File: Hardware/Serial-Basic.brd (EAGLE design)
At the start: 22.9 x 17.3 mm, 24 parts, among them J1 microB, U1 AP2112-3.3V, U2 CH340G, Y2 12MHz

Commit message: Adding buffer to RX line.
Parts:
- added U4: 7408, Serial-Basic:SOT353
- moved JP3 14.9 mm to (3.81, 16.0)
- moved JP4 12.8 mm to (21.5, 1.40)
- moved LOGO3 0.38 mm to (8.89, -0.13)
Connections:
- new net N$5: D2.C, U4.4
- new net SHLD: J1.SHIELD1, J1.SHIELD2, J1.SHIELD3
- net GND: now also U4.3
- net RXI: now also U4.1, U4.2; no longer D2.C
- net VCC: now also U4.5
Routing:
- net VCC: track 49.9 -> 44.2 mm
- net N$5: track 0.00 -> 1.95 mm
- net RXI: track 27.5 -> 29.0 mm
- net TXO: track 24.5 -> 25.1 mm
- net GND: vias 9 -> 11

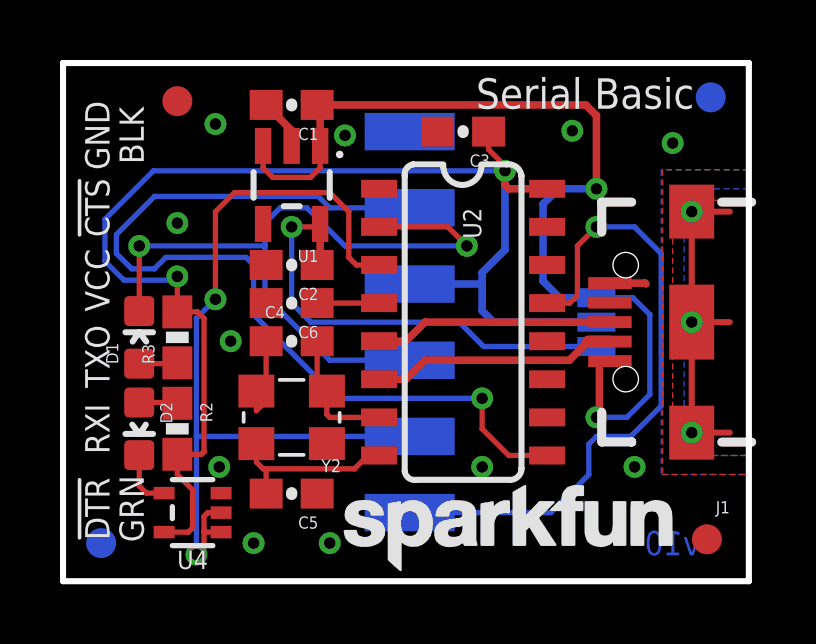
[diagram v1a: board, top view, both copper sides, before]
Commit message: Adding PROD_ID to AND gate
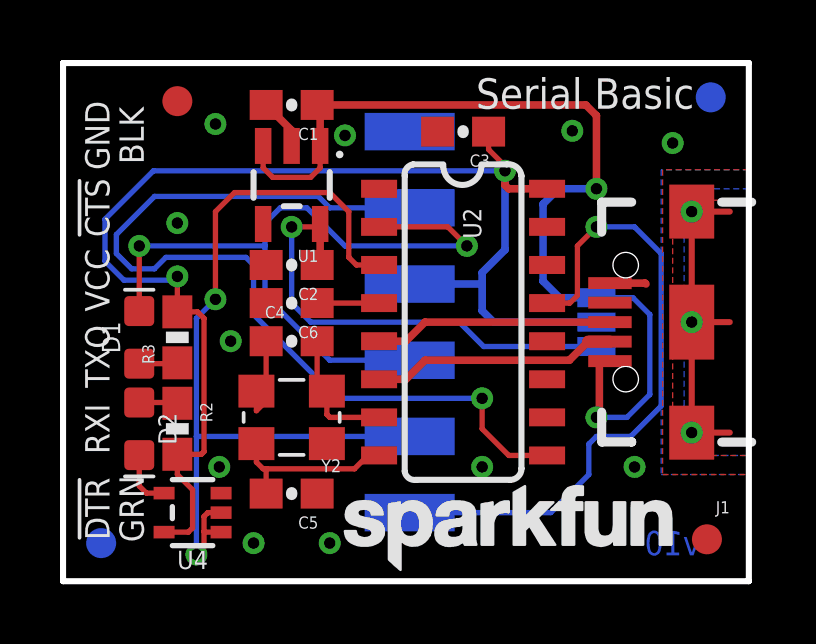
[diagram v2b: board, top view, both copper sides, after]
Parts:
- U4: value 7408 -> 74LVC1G08SE
- turned D1 to 90 degrees
- turned D2 to 270 degrees
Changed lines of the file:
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@@
 <?xml version="1.0" encoding="utf-8"?>
 <!DOCTYPE eagle SYSTEM "eagle.dtd">
-<eagle version="7.6.0">
+<eagle version="7.2.0">
 <drawing>
 <settings>
@@
 <layer number="20" name="Dimension" color="15" fill="1" visible="yes" active="yes"/>
 <layer number="21" name="tPlace" color="16" fill="1" visible="yes" active="yes"/>
-<layer number="22" name="bPlace" color="14" fill="1" visible="no" active="yes"/>
+<layer number="22" name="bPlace" color="14" fill="1" visible="yes" active="yes"/>
 <layer number="23" name="tOrigins" color="15" fill="1" visible="yes" active="yes"/>
-<layer number="24" name="bOrigins" color="15" fill="1" visible="no" active="yes"/>
-<layer number="25" name="tNames" color="7" fill="1" visible="yes" active="yes"/>
+<layer number="24" name="bOrigins" color="15" fill="1" visible="yes" active="yes"/>
+<layer number="25" name="tNames" color="7" fill="1" visible="no" active="yes"/>
 <layer number="26" name="bNames" color="7" fill="1" visible="no" active="yes"/>
 <layer number="27" name="tValues" color="7" fill="1" visible="no" active="yes"/>
@@
 <layer number="43" name="vRestrict" color="2" fill="10" visible="no" active="yes"/>
 <layer number="44" name="Drills" color="7" fill="1" visible="no" active="yes"/>
-<layer number="45" name="Holes" color="7" fill="1" visible="no" active="yes"/>
+<layer number="45" name="Holes" color="7" fill="1" visible="yes" active="yes"/>
 <layer number="46" name="Milling" color="3" fill="1" visible="no" active="yes"/>
 <layer number="47" name="Measures" color="7" fill="1" visible="no" active="yes"/>
@@
 <layer number="49" name="Reference" color="7" fill="1" visible="no" active="yes"/>
 <layer number="50" name="dxf" color="7" fill="1" visible="no" active="yes"/>
-<layer number="51" name="tDocu" color="6" fill="1" visible="no" active="yes"/>
+<layer number="51" name="tDocu" color="6" fill="1" visible="yes" active="yes"/>
 <layer number="52" name="bDocu" color="7" fill="1" visible="no" active="yes"/>
 <layer number="53" name="tGND_GNDA" color="7" fill="9" visible="no" active="no"/>
@@
 <element name="LOGO3" library="SparkFun-Aesthetics" package="SFE_LOGO_NAME_.1" value="SFE_LOGO_NAME.1_INCH" x="8.89" y="-0.127"/>
 <element name="LOGO2" library="SparkFun-Aesthetics" package="SFE_LOGO_FLAME_.1" value="SFE_LOGO_FLAME.1_INCH" x="22.479" y="7.874" rot="MR270"/>
-<element name="D1" library="SparkFun-LED" package="LED-0603" value="GREEN" x="2.54" y="8.128">
-<attribute name="PROD_ID" value="DIO-00821" x="2.54" y="8.128" size="1.27" layer="27" font="vector" ratio="15" display="off"/>
-</element>
-<element name="D2" library="SparkFun-LED" package="LED-0603" value="Yellow" x="2.54" y="5.08" rot="R180">
-<attribute name="PROD_ID" value="DIO-09003" x="2.54" y="5.08" size="1.27" layer="27" font="vector" ratio="15" rot="R180" display="off"/>
+<element name="D1" library="SparkFun-LED" package="LED-0603" value="GREEN" x="2.54" y="8.128" rot="R90">
+<attribute name="PROD_ID" value="DIO-00821" x="2.54" y="8.128" size="1.27" layer="27" font="vector" ratio="15" rot="R90" display="off"/>
+</element>
+<element name="D2" library="SparkFun-LED" package="LED-0603" value="Yellow" x="2.54" y="5.08" rot="R270">
+<attribute name="PROD_ID" value="DIO-09003" x="2.54" y="5.08" size="1.27" layer="27" font="vector" ratio="15" rot="R270" display="off"/>
 </element>
 <element name="R2" library="SparkFun-Resistors" package="0603-RES" value="1K" x="3.81" y="5.08" rot="R270">
@@
 <attribute name="PROD_ID" value="RES-00818" x="3.81" y="8.128" size="1.778" layer="27" font="vector" ratio="15" rot="R90" display="off"/>
 </element>
-<element name="U4" library="Serial-Basic" package="SOT353" value="7408" x="4.318" y="2.286" rot="R90"/>
+<element name="U4" library="Serial-Basic" package="SOT353" value="74LVC1G08SE" x="4.318" y="2.286" rot="R90">
+<attribute name="PROD_ID" value="IC-10841" x="4.318" y="2.286" size="1.778" layer="27" rot="R90" display="off"/>
+<attribute name="VALUE" value="74LVC1G08SE" x="4.318" y="2.286" size="1.778" layer="27" rot="R90" display="off"/>
+</element>
 </elements>
 <signals>
